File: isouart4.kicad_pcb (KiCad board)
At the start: 2 copper layers, 89 x 99 mm, 40 parts, among them J1 USB_B, J2 Conn_01x04, J3 Conn_01x04, J4 Conn_01x04, J5 Conn_01x04, U1 FT4232H, U10 74HC123, U11 74HC123, U12 74HC123, U13 74HC123, U2 93LCxxB, U3 AMS1117-3.3, U5 74HC595D, U6 π122U31, U7 π122U31, U8 π122U31, U9 π122U31, Y1 12.000 MHz

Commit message: Flush
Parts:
- added C10: 3.3uF, Capacitor_SMD:C_0805_2012Metric_Pad1.18x1.45mm_HandSolder, F.Cu at (166.9, 76.6)
- added C11: 3.3uF, Capacitor_SMD:C_0805_2012Metric_Pad1.18x1.45mm_HandSolder, F.Cu at (156.2, 73.5)
- added C12: 3.3uF, Capacitor_SMD:C_0805_2012Metric_Pad1.18x1.45mm_HandSolder, F.Cu at (166.1, 88.4)
- added C13: 1uF, Capacitor_SMD:C_0805_2012Metric_Pad1.18x1.45mm_HandSolder, F.Cu at (209.7, 64.0)
- added C14: 1uF, Capacitor_SMD:C_0805_2012Metric_Pad1.18x1.45mm_HandSolder, F.Cu at (213.9, 82.2)
- added C15: 1uF, Capacitor_SMD:C_0805_2012Metric_Pad1.18x1.45mm_HandSolder, F.Cu at (208.5, 90.9)
- added C16: 1uF, Capacitor_SMD:C_0805_2012Metric_Pad1.18x1.45mm_HandSolder, F.Cu at (210.4, 108.7)
- added C17: 1uF, Capacitor_SMD:C_0805_2012Metric_Pad1.18x1.45mm_HandSolder, F.Cu at (204.8, 62.5)
- added C18: 1uF, Capacitor_SMD:C_0805_2012Metric_Pad1.18x1.45mm_HandSolder, F.Cu at (213.9, 85.2)
- added C19: 1uF, Capacitor_SMD:C_0805_2012Metric_Pad1.18x1.45mm_HandSolder, F.Cu at (208.5, 93.9)
- added C20: 1uF, Capacitor_SMD:C_0805_2012Metric_Pad1.18x1.45mm_HandSolder, F.Cu at (210.4, 111.7)
- added C21: 1uF, Capacitor_SMD:C_0805_2012Metric_Pad1.18x1.45mm_HandSolder, B.Cu at (207.0, 68.8)
- added C22: 1uF, Capacitor_SMD:C_0805_2012Metric_Pad1.18x1.45mm_HandSolder, F.Cu at (205.1, 79.9)
- added C23: 1uF, Capacitor_SMD:C_0805_2012Metric_Pad1.18x1.45mm_HandSolder, F.Cu at (208.5, 96.9)
- added C24: 1uF, Capacitor_SMD:C_0805_2012Metric_Pad1.18x1.45mm_HandSolder, F.Cu at (210.4, 114.7)
- added C7: 3.3uF, Capacitor_SMD:C_0805_2012Metric_Pad1.18x1.45mm_HandSolder, F.Cu at (150.9, 79.8)
- added C8: 3.3uF, Capacitor_SMD:C_0805_2012Metric_Pad1.18x1.45mm_HandSolder, F.Cu at (160.3, 75.2)
- added C9: 3.3uF, Capacitor_SMD:C_0805_2012Metric_Pad1.18x1.45mm_HandSolder, F.Cu at (167.0, 84.7)
- added R10: 1k, Resistor_SMD:R_0805_2012Metric_Pad1.20x1.40mm_HandSolder, F.Cu at (205.7, 111.6)
- added R11: 220k, Resistor_SMD:R_0805_2012Metric_Pad1.20x1.40mm_HandSolder, F.Cu at (209.6, 59.8)
- added R12: 220k, Resistor_SMD:R_0805_2012Metric_Pad1.20x1.40mm_HandSolder, F.Cu at (200.3, 79.7)
- added R13: 220k, Resistor_SMD:R_0805_2012Metric_Pad1.20x1.40mm_HandSolder, F.Cu at (203.7, 96.8)
- added R14: 220k, Resistor_SMD:R_0805_2012Metric_Pad1.20x1.40mm_HandSolder, F.Cu at (205.7, 114.6)
- added R15: 220k, Resistor_SMD:R_0805_2012Metric_Pad1.20x1.40mm_HandSolder, F.Cu at (204.7, 58.1)
- added R16: 220k, Resistor_SMD:R_0805_2012Metric_Pad1.20x1.40mm_HandSolder, F.Cu at (200.3, 82.7)
- added R17: 220k, Resistor_SMD:R_0805_2012Metric_Pad1.20x1.40mm_HandSolder, F.Cu at (216.2, 103.5)
- added R18: 220k, Resistor_SMD:R_0805_2012Metric_Pad1.20x1.40mm_HandSolder, F.Cu at (205.7, 117.5)
- added R2: 1k, Resistor_SMD:R_0805_2012Metric_Pad1.20x1.40mm_HandSolder, F.Cu at (213.4, 51.8)
- added R4: 1k, Resistor_SMD:R_0805_2012Metric_Pad1.20x1.40mm_HandSolder, F.Cu at (209.1, 82.2)
- added R5: 1k, Resistor_SMD:R_0805_2012Metric_Pad1.20x1.40mm_HandSolder, F.Cu at (203.7, 90.9)
- added R6: 1k, Resistor_SMD:R_0805_2012Metric_Pad1.20x1.40mm_HandSolder, F.Cu at (205.7, 108.7)
- added R7: 1k, Resistor_SMD:R_0805_2012Metric_Pad1.20x1.40mm_HandSolder, F.Cu at (199.7, 51.8)
- added R8: 1k, Resistor_SMD:R_0805_2012Metric_Pad1.20x1.40mm_HandSolder, F.Cu at (209.1, 85.2)
- added R9: 1k, Resistor_SMD:R_0805_2012Metric_Pad1.20x1.40mm_HandSolder, F.Cu at (203.7, 93.8)
- C1, C2, C3, C4, C5, C6, L1, L2, R1, R3: moved to F.Cu
- U10, U11, U12, U13: moved to B.Cu
- moved D5 70.3 mm to (204.5, 50.8), turned to 0 degrees
- moved U13 60.3 mm to (207.9, 111.6), turned to 90 degrees
- moved D8 58.4 mm to (206.5, 121.7), turned to -90 degrees
- moved U10 51.6 mm to (207.1, 61.6)
- moved D6 31.8 mm to (204.4, 73.4), turned to 0 degrees
- moved U12 22.1 mm to (206.8, 94.1), turned to 90 degrees
- moved C6 17.2 mm to (150.9, 85.3), turned to 0 degrees
- moved J5 17.0 mm to (220.9, 124.4), turned to 90 degrees
- moved D7 15.7 mm to (206.9, 99.8), turned to -90 degrees
- moved J4 13.4 mm to (220.7, 103.7), turned to 90 degrees
- moved U11 9.65 mm to (207.1, 83.0), turned to -90 degrees
- moved C2 9.21 mm to (175.9, 89.9), turned to 180 degrees
- moved L2 8.83 mm to (172.4, 95.8)
- moved C3 7.21 mm to (156.3, 88.9), turned to 0 degrees
- moved C1 6.83 mm to (175.9, 85.0), turned to 180 degrees
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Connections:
- D5 pad 1: unconnected-(D5-K1-Pad1) -> Net-(D5-K1)
- D5 pad 2: unconnected-(D5-A-Pad2) -> /indicators-ch1/V+MON
- D5 pad 3: unconnected-(D5-K2-Pad3) -> Net-(D5-K2)
- D6 pad 1: unconnected-(D6-K1-Pad1) -> Net-(D6-K1)
- D6 pad 2: unconnected-(D6-A-Pad2) -> /indicators-ch2/V+MON
- D6 pad 3: unconnected-(D6-K2-Pad3) -> Net-(D6-K2)
- D7 pad 1: unconnected-(D7-K1-Pad1) -> Net-(D7-K1)
- D7 pad 2: unconnected-(D7-A-Pad2) -> /indicators-ch3/V+MON
- D7 pad 3: unconnected-(D7-K2-Pad3) -> Net-(D7-K2)
- D8 pad 1: unconnected-(D8-K1-Pad1) -> Net-(D8-K1)
- D8 pad 2: unconnected-(D8-A-Pad2) -> /indicators-ch4/V+MON
- D8 pad 3: unconnected-(D8-K2-Pad3) -> Net-(D8-K2)
- J2 pad 2: Net-(J2-Pin_2) -> /indicators-ch1/TXMON
- J2 pad 3: Net-(J2-Pin_3) -> /indicators-ch1/RXMON
- J2 pad 4: Net-(J2-Pin_4) -> /indicators-ch1/V+MON
- J3 pad 1: Net-(J3-Pin_1) -> /indicators-ch2/GNDMON
- J3 pad 2: Net-(J3-Pin_2) -> /indicators-ch2/TXMON
- J3 pad 3: Net-(J3-Pin_3) -> /indicators-ch2/RXMON
- J3 pad 4: Net-(J3-Pin_4) -> /indicators-ch2/V+MON
- J4 pad 1: Net-(J4-Pin_1) -> /indicators-ch3/GNDMON
- J4 pad 2: Net-(J4-Pin_2) -> /indicators-ch3/TXMON
- J4 pad 3: Net-(J4-Pin_3) -> /indicators-ch3/RXMON
- J4 pad 4: Net-(J4-Pin_4) -> /indicators-ch3/V+MON
- J5 pad 1: Net-(J5-Pin_1) -> /indicators-ch4/GNDMON
- J5 pad 2: Net-(J5-Pin_2) -> /indicators-ch4/TXMON
- J5 pad 3: Net-(J5-Pin_3) -> /indicators-ch4/RXMON
- J5 pad 4: Net-(J5-Pin_4) -> /indicators-ch4/V+MON
- U10 pad 1: unconnected-(U10A-A-Pad1) -> /indicators-ch1/TXMON
- U10 pad 10: unconnected-(U10B-B-Pad10) -> /indicators-ch1/V+MON
- U10 pad 11: unconnected-(U10B-Clr-Pad11) -> /indicators-ch1/V+MON
- U10 pad 12: unconnected-(U10B-~{Q}-Pad12) -> Net-(U10B-~{Q})
- U10 pad 14: unconnected-(U10A-Cext-Pad14) -> Net-(U10A-Cext)
- U10 pad 15: unconnected-(U10A-RCext-Pad15) -> Net-(U10A-RCext)
- U10 pad 16: unconnected-(U10C-VCC-Pad16) -> /indicators-ch1/V+MON
- U10 pad 2: unconnected-(U10A-B-Pad2) -> /indicators-ch1/V+MON
- U10 pad 3: unconnected-(U10A-Clr-Pad3) -> /indicators-ch1/V+MON
- U10 pad 4: unconnected-(U10A-~{Q}-Pad4) -> Net-(U10A-~{Q})
- U10 pad 6: unconnected-(U10B-Cext-Pad6) -> Net-(U10B-Cext)
- U10 pad 7: unconnected-(U10B-RCext-Pad7) -> Net-(U10B-RCext)
- U10 pad 8: unconnected-(U10C-GND-Pad8) -> /indicators-ch1/GNDMON
- U10 pad 9: unconnected-(U10B-A-Pad9) -> /indicators-ch1/RXMON
- U11 pad 1: unconnected-(U11A-A-Pad1) -> /indicators-ch2/TXMON
- U11 pad 10: unconnected-(U11B-B-Pad10) -> /indicators-ch2/V+MON
- U11 pad 11: unconnected-(U11B-Clr-Pad11) -> /indicators-ch2/V+MON
- U11 pad 12: unconnected-(U11B-~{Q}-Pad12) -> Net-(U11B-~{Q})
- U11 pad 14: unconnected-(U11A-Cext-Pad14) -> Net-(U11A-Cext)
- U11 pad 15: unconnected-(U11A-RCext-Pad15) -> Net-(U11A-RCext)
- U11 pad 16: unconnected-(U11C-VCC-Pad16) -> /indicators-ch2/V+MON
- U11 pad 2: unconnected-(U11A-B-Pad2) -> /indicators-ch2/V+MON
- U11 pad 3: unconnected-(U11A-Clr-Pad3) -> /indicators-ch2/V+MON
- U11 pad 4: unconnected-(U11A-~{Q}-Pad4) -> Net-(U11A-~{Q})
- U11 pad 6: unconnected-(U11B-Cext-Pad6) -> Net-(U11B-Cext)
- U11 pad 7: unconnected-(U11B-RCext-Pad7) -> Net-(U11B-RCext)
- U11 pad 8: unconnected-(U11C-GND-Pad8) -> /indicators-ch2/GNDMON
- U11 pad 9: unconnected-(U11B-A-Pad9) -> /indicators-ch2/RXMON
- U12 pad 1: unconnected-(U12A-A-Pad1) -> /indicators-ch3/TXMON
- U12 pad 10: unconnected-(U12B-B-Pad10) -> /indicators-ch3/V+MON
- U12 pad 11: unconnected-(U12B-Clr-Pad11) -> /indicators-ch3/V+MON
- U12 pad 12: unconnected-(U12B-~{Q}-Pad12) -> Net-(U12B-~{Q})
- U12 pad 14: unconnected-(U12A-Cext-Pad14) -> Net-(U12A-Cext)
- U12 pad 15: unconnected-(U12A-RCext-Pad15) -> Net-(U12A-RCext)
- U12 pad 16: unconnected-(U12C-VCC-Pad16) -> /indicators-ch3/V+MON
- U12 pad 2: unconnected-(U12A-B-Pad2) -> /indicators-ch3/V+MON
- U12 pad 3: unconnected-(U12A-Clr-Pad3) -> /indicators-ch3/V+MON
- U12 pad 4: unconnected-(U12A-~{Q}-Pad4) -> Net-(U12A-~{Q})
- U12 pad 6: unconnected-(U12B-Cext-Pad6) -> Net-(U12B-Cext)
- U12 pad 7: unconnected-(U12B-RCext-Pad7) -> Net-(U12B-RCext)
- U12 pad 8: unconnected-(U12C-GND-Pad8) -> /indicators-ch3/GNDMON
- U12 pad 9: unconnected-(U12B-A-Pad9) -> /indicators-ch3/RXMON
- U13 pad 1: unconnected-(U13A-A-Pad1) -> /indicators-ch4/TXMON
- U13 pad 10: unconnected-(U13B-B-Pad10) -> /indicators-ch4/V+MON
- U13 pad 11: unconnected-(U13B-Clr-Pad11) -> /indicators-ch4/V+MON
- U13 pad 12: unconnected-(U13B-~{Q}-Pad12) -> Net-(U13B-~{Q})
- U13 pad 14: unconnected-(U13A-Cext-Pad14) -> Net-(U13A-Cext)
- U13 pad 15: unconnected-(U13A-RCext-Pad15) -> Net-(U13A-RCext)
- U13 pad 16: unconnected-(U13C-VCC-Pad16) -> /indicators-ch4/V+MON
- U13 pad 2: unconnected-(U13A-B-Pad2) -> /indicators-ch4/V+MON
- U13 pad 3: unconnected-(U13A-Clr-Pad3) -> /indicators-ch4/V+MON
- U13 pad 4: unconnected-(U13A-~{Q}-Pad4) -> Net-(U13A-~{Q})
- U13 pad 6: unconnected-(U13B-Cext-Pad6) -> Net-(U13B-Cext)
- U13 pad 7: unconnected-(U13B-RCext-Pad7) -> Net-(U13B-RCext)
- U13 pad 8: unconnected-(U13C-GND-Pad8) -> /indicators-ch4/GNDMON
- U13 pad 9: unconnected-(U13B-A-Pad9) -> /indicators-ch4/RXMON
- U6 pad 6: Net-(J2-Pin_2) -> /indicators-ch1/TXMON
- U6 pad 7: Net-(J2-Pin_3) -> /indicators-ch1/RXMON
- U6 pad 8: Net-(J2-Pin_4) -> /indicators-ch1/V+MON
- U7 pad 5: Net-(J3-Pin_1) -> /indicators-ch2/GNDMON
- U7 pad 6: Net-(J3-Pin_2) -> /indicators-ch2/TXMON
- U7 pad 7: Net-(J3-Pin_3) -> /indicators-ch2/RXMON
- U7 pad 8: Net-(J3-Pin_4) -> /indicators-ch2/V+MON
- U8 pad 5: Net-(J4-Pin_1) -> /indicators-ch3/GNDMON
- U8 pad 6: Net-(J4-Pin_2) -> /indicators-ch3/TXMON
- U8 pad 7: Net-(J4-Pin_3) -> /indicators-ch3/RXMON
- U8 pad 8: Net-(J4-Pin_4) -> /indicators-ch3/V+MON
- U9 pad 5: Net-(J5-Pin_1) -> /indicators-ch4/GNDMON
- U9 pad 6: Net-(J5-Pin_2) -> /indicators-ch4/TXMON
- U9 pad 7: Net-(J5-Pin_3) -> /indicators-ch4/RXMON
- U9 pad 8: Net-(J5-Pin_4) -> /indicators-ch4/V+MON
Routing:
- net /indicators-ch1/V+MON: track 0.00 -> 77.1 mm, vias 0 -> 4
- net /indicators-ch1/TXMON: track 0.00 -> 31.6 mm, vias 0 -> 2
- net /indicators-ch1/RXMON: track 0.00 -> 29.8 mm, vias 0 -> 2
- net Net-(J2-Pin_1): track 0.00 -> 29.1 mm, vias 0 -> 2
- net /USB2-UART4/TX1: track 107.5 -> 91.4 mm
- net Net-(U10B-~{Q}): track 0.00 -> 12.1 mm, vias 0 -> 1
- net Net-(U10A-~{Q}): track 0.00 -> 11.2 mm, vias 0 -> 1
- net Net-(U10B-RCext): track 0.00 -> 9.83 mm, vias 0 -> 1
- net /indicators-ch1/GNDMON: track 0.00 -> 9.62 mm
- net /USB2-UART4/VIN 3.3V: track 278.8 -> 269.5 mm, vias 10 -> 11
- net Net-(U1-VREGOUT): track 54.2 -> 46.7 mm, vias 5 -> 4
- net Net-(U10A-RCext): track 0.00 -> 7.01 mm, vias 0 -> 1
- net Net-(U10A-Cext): track 0.00 -> 6.71 mm, vias 0 -> 1
- net /USB2-UART4/VPLL +3.3V: track 17.8 -> 12.1 mm, vias 0 -> 1
- net GND: track 81.9 -> 76.6 mm, vias 18 -> 13
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
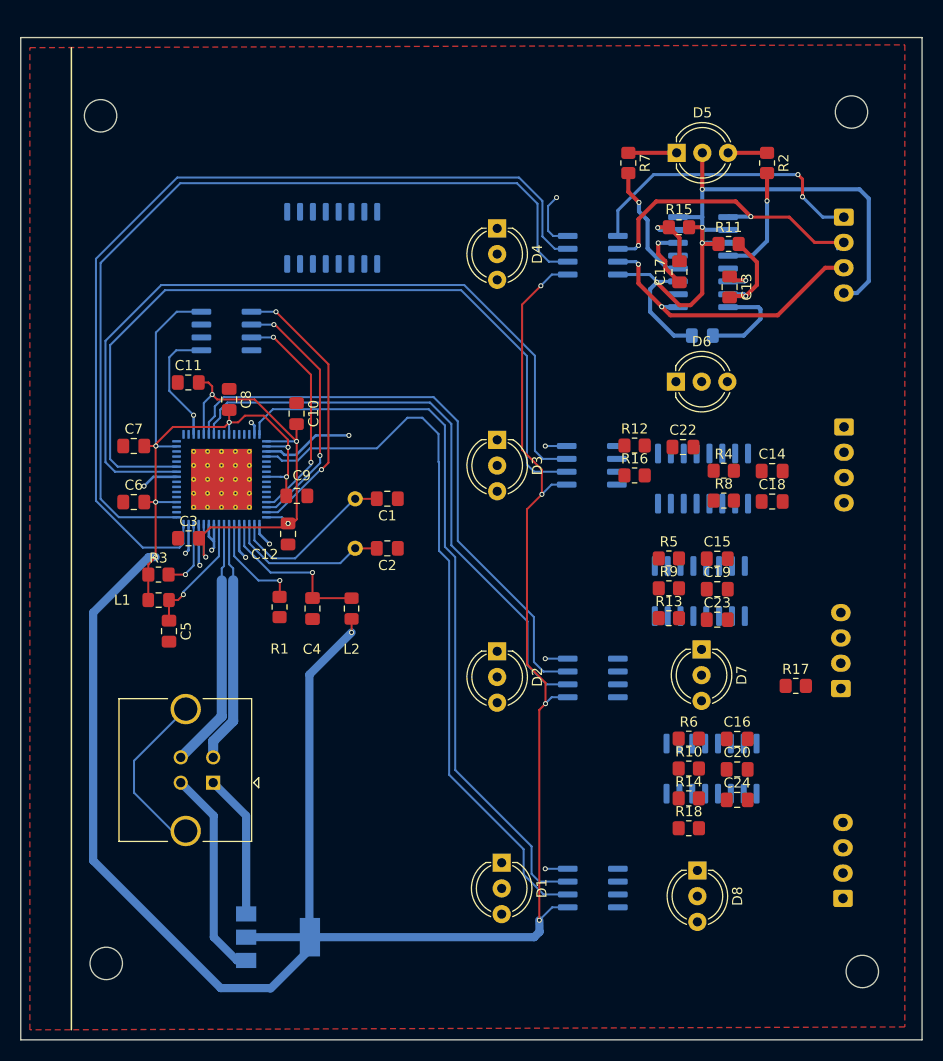
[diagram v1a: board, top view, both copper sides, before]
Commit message: switch to CH344Q
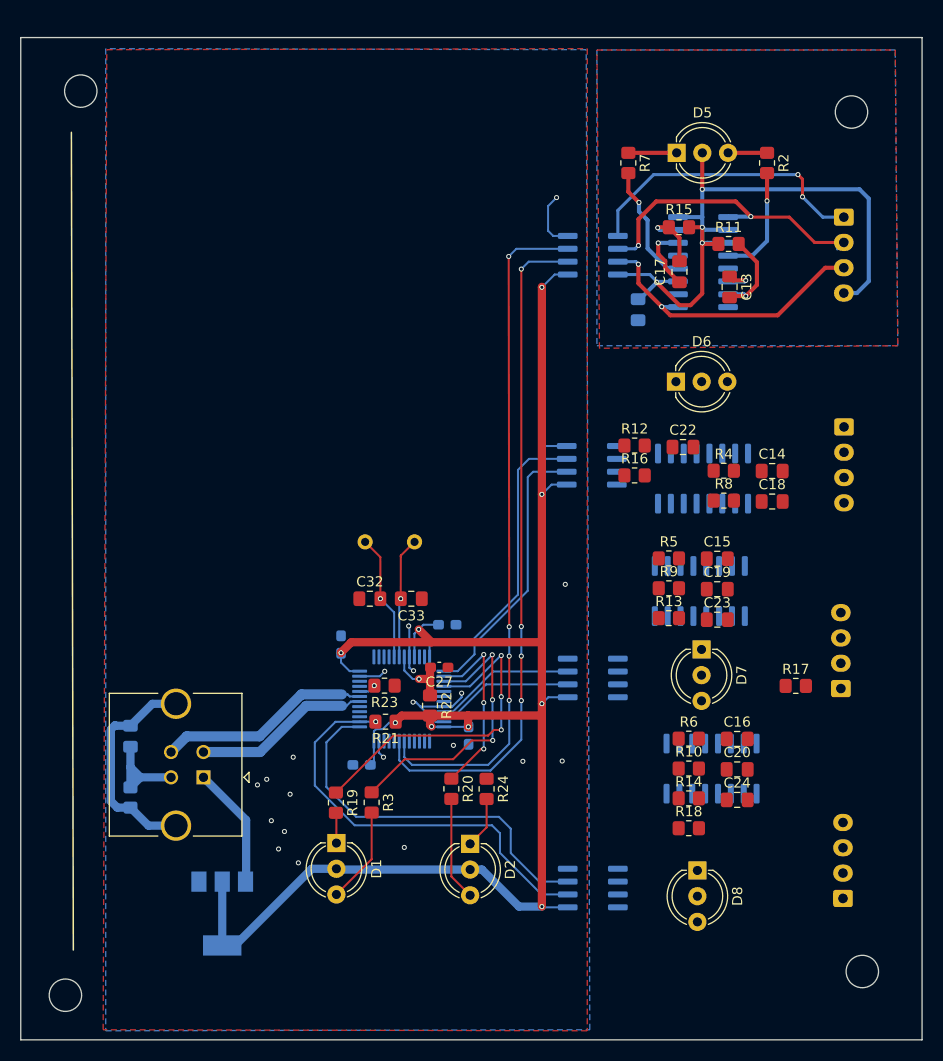
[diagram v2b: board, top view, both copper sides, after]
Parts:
- removed C10, C11, C12, C3, C4, C5, C6, C7, C8, C9: 3.3uF, Capacitor_SMD:C_0805_2012Metric_Pad1.18x1.45mm_HandSolder
- removed C2: 30pF, Capacitor_SMD:C_0805_2012Metric_Pad1.18x1.45mm_HandSolder
- removed D3, D4: LED_Dual_KAK, LED_THT:LED_D5.0mm-3
- removed L1, L2: L_Iron, Inductor_SMD:L_0805_2012Metric_Pad1.15x1.40mm_HandSolder
- removed U2: 93LCxxB, Package_SO:SOIC-8_3.9x4.9mm_P1.27mm
- removed U5: 74HC595D, Package_SO:SO-16_3.9x9.9mm_P1.27mm
- removed Y1: 12.000 MHz, Crystal:Crystal_HC49-U_Vertical
- added C27: 100n, Capacitor_SMD:C_0603_1608Metric_Pad1.08x0.95mm_HandSolder, F.Cu at (181.0, 101.6)
- added C28: 100n, Capacitor_SMD:C_0603_1608Metric_Pad1.08x0.95mm_HandSolder, B.Cu at (181.8, 97.4)
- added C29: 100n, Capacitor_SMD:C_0603_1608Metric_Pad1.08x0.95mm_HandSolder, B.Cu at (183.9, 108.4)
- added C30: 100n, Capacitor_SMD:C_0603_1608Metric_Pad1.08x0.95mm_HandSolder, B.Cu at (173.4, 111.3)
- added C31: 100n, Capacitor_SMD:C_0603_1608Metric_Pad1.08x0.95mm_HandSolder, B.Cu at (171.3, 99.4)
- added C32: 22p, Capacitor_SMD:C_0805_2012Metric_Pad1.18x1.45mm_HandSolder, F.Cu at (174.2, 94.8)
- added C33: 22p, Capacitor_SMD:C_0805_2012Metric_Pad1.18x1.45mm_HandSolder, F.Cu at (178.3, 94.8)
- added R19: 1k, Resistor_SMD:R_0805_2012Metric_Pad1.20x1.40mm_HandSolder, F.Cu at (170.8, 115.0)
- added R20: 1k, Resistor_SMD:R_0805_2012Metric_Pad1.20x1.40mm_HandSolder, F.Cu at (182.2, 113.6)
- added R21: 4k7, Resistor_SMD:R_0805_2012Metric_Pad1.20x1.40mm_HandSolder, F.Cu at (175.7, 107.0)
- added R22: 4k7, Resistor_SMD:R_0805_2012Metric_Pad1.20x1.40mm_HandSolder, F.Cu at (180.1, 105.4)
- added R23: 4k7, Resistor_SMD:R_0805_2012Metric_Pad1.20x1.40mm_HandSolder, F.Cu at (175.6, 103.4)
- added R24: 1k, Resistor_SMD:R_0805_2012Metric_Pad1.20x1.40mm_HandSolder, F.Cu at (185.7, 113.6)
- added Y2: 8MHz, Crystal:Crystal_HC49-U_Vertical, B.Cu at (173.7, 89.2)
- C1: value 30pF -> 4n7; moved to B.Cu
- R1: value 12k 1% -> 1M; moved to B.Cu
- U1: value FT4232H -> CH344Q; footprint Package_DFN_QFN:QFN-64-1EP_9x9mm_P0.5mm_EP6x6mm_ThermalVias -> Package_QFP:LQFP-48_7x7mm_P0.5mm
- moved C1 34.6 mm to (150.5, 108.4), turned to 90 degrees
- moved R3 30.8 mm to (174.3, 115.0), turned to -90 degrees
- moved U1 28.1 mm to (177.3, 104.7), turned to -90 degrees
- moved R1 23.9 mm to (150.5, 114.5)
- moved D2 19.2 mm to (184.1, 119.0)
- moved D1 16.4 mm to (170.9, 119.0)
- moved C21 6.85 mm to (200.7, 66.3), turned to 90 degrees
- moved U3 5.99 mm to (159.6, 125.9), turned to -90 degrees
- moved H1 5.11 mm to (144.1, 134.0)
- moved H4 3.13 mm to (145.6, 44.7)
- moved J1 1.09 mm to (157.7, 112.5)
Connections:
- C1 pad 2: Net-(U1-OSCI) -> Net-(J1-Shield)
- D1 pad 1: unconnected-(D1-K1-Pad1) -> Net-(D1-K1)
- D1 pad 2: unconnected-(D1-A-Pad2) -> /USB-UART4-CH344Q/VIN 3.3V
- D1 pad 3: unconnected-(D1-K2-Pad3) -> Net-(D1-K2)
- D2 pad 1: unconnected-(D2-K1-Pad1) -> Net-(D2-K1)
- D2 pad 2: unconnected-(D2-A-Pad2) -> /USB-UART4-CH344Q/VIN 3.3V
- D2 pad 3: unconnected-(D2-K2-Pad3) -> Net-(D2-K2)
- J1 pad 2: /USB2-UART4/D- -> /USB-UART4-CH344Q/USB_N
- J1 pad 3: /USB2-UART4/D+ -> /USB-UART4-CH344Q/USB_P
- J1 pad 5: unconnected-(J1-Shield-Pad5) -> Net-(J1-Shield)
- J2 pad 1: Net-(J2-Pin_1) -> /indicators-ch1/GNDMON
- R1 pad 1: Net-(U1-REF) -> GND
- R1 pad 2: GND -> Net-(J1-Shield)
- R3 pad 1: /USB2-UART4/VIN 3.3V -> /USB-UART4-CH344Q/TX_S
- R3 pad 2: Net-(U1-~{RESET}) -> Net-(D1-K2)
- U1 pad 1: GND -> unconnected-(U1A-NC-Pad1)
- U1 pad 10: GND -> unconnected-(U1C-GPIO2|CTS1-Pad10)
- U1 pad 11: GND -> unconnected-(U1C-GPIO3|RTS1-Pad11)
- U1 pad 12: Net-(U1-VREGOUT) -> /USB-UART4-CH344Q/TXD1_INT
- U1 pad 13: GND -> /USB-UART4-CH344Q/RXD1_INT
- U1 pad 14: Net-(U1-~{RESET}) -> /USB-UART4-CH344Q/ACT
- U1 pad 15: GND -> /USB-UART4-CH344Q/TX_S
- U1 pad 16: /USB2-UART4/TX1 -> /USB-UART4-CH344Q/RX_S
- U1 pad 17: /USB2-UART4/RX1 -> unconnected-(U1C-DSR1-Pad17)
- U1 pad 2: Net-(U1-OSCI) -> unconnected-(U1D-DSR2-Pad2)
- U1 pad 20: /USB2-UART4/VIN 3.3V -> GND
- U1 pad 21: unconnected-(U1-ADBUS4-Pad21) -> /USB-UART4-CH344Q/TXD2_INT
- U1 pad 22: unconnected-(U1-ADBUS5-Pad22) -> /USB-UART4-CH344Q/RXD2_INT
- U1 pad 23: unconnected-(U1-ADBUS6-Pad23) -> GND
- U1 pad 24: unconnected-(U1-ADBUS7-Pad24) -> /USB-UART4-CH344Q/VIN 3.3V
- U1 pad 25: GND -> unconnected-(U1C-RI1-Pad25)
- U1 pad 26: /USB2-UART4/TX2 -> unconnected-(U1D-GPIO4|CTS2-Pad26)
- U1 pad 27: /USB2-UART4/RX2 -> unconnected-(U1D-GPIO5|RTS2-Pad27)
- U1 pad 3: Net-(U1-OSCO) -> unconnected-(U1D-RI2-Pad3)
- U1 pad 30: unconnected-(U1-BDBUS4-Pad30) -> /USB-UART4-CH344Q/TXD0_INT
- U1 pad 31: /USB2-UART4/VIN 3.3V -> /USB-UART4-CH344Q/RXD0_INT
- U1 pad 36: unconnected-(U1-~{SUSPEND}-Pad36) -> /USB-UART4-CH344Q/VIN 3.3V
- U1 pad 37: Net-(U1-VREGOUT) -> /USB-UART4-CH344Q/TXD3_INT
- U1 pad 38: /USB2-UART4/TX3 -> /USB-UART4-CH344Q/RXD3_INT
- U1 pad 39: /USB2-UART4/RX3 -> unconnected-(U1B-GPIO8|TNOW0|DTR0-Pad39)
- U1 pad 4: /USB2-UART4/VPHY +3.3V -> unconnected-(U1D-DCD2-Pad4)
- U1 pad 42: /USB2-UART4/VIN 3.3V -> /USB-UART4-CH344Q/USB_N
- U1 pad 43: unconnected-(U1-CDBUS4-Pad43) -> /USB-UART4-CH344Q/USB_P
- U1 pad 44: unconnected-(U1-CDBUS5-Pad44) -> /USB-UART4-CH344Q/TEST
- U1 pad 48: /USB2-UART4/TX4 -> /USB-UART4-CH344Q/VIN 3.3V
- U1 pad 5: GND -> /USB-UART4-CH344Q/XI
- U1 pad 6: Net-(U1-REF) -> /USB-UART4-CH344Q/XO
- U1 pad 7: /USB2-UART4/D- -> /USB-UART4-CH344Q/RESET
- U1 pad 8: /USB2-UART4/D+ -> GND
- U1 pad 9: /USB2-UART4/VPLL +3.3V -> /USB-UART4-CH344Q/VIN 3.3V
- U3 pad 2: /USB2-UART4/VIN 3.3V -> /USB-UART4-CH344Q/VIN 3.3V
- U6 pad 1: /USB2-UART4/VIN 3.3V -> /USB-UART4-CH344Q/VIN 3.3V
- U6 pad 2: /USB2-UART4/RX1 -> /USB-UART4-CH344Q/RXD0_INT
- U6 pad 3: /USB2-UART4/TX1 -> /USB-UART4-CH344Q/TXD0_INT
- U6 pad 5: Net-(J2-Pin_1) -> /indicators-ch1/GNDMON
- U7 pad 1: /USB2-UART4/VIN 3.3V -> /USB-UART4-CH344Q/VIN 3.3V
- U7 pad 2: /USB2-UART4/RX2 -> /USB-UART4-CH344Q/RXD1_INT
- U7 pad 3: /USB2-UART4/TX2 -> /USB-UART4-CH344Q/TXD1_INT
- U8 pad 1: /USB2-UART4/VIN 3.3V -> /USB-UART4-CH344Q/VIN 3.3V
- U8 pad 2: /USB2-UART4/RX3 -> /USB-UART4-CH344Q/RXD2_INT
- U8 pad 3: /USB2-UART4/TX3 -> /USB-UART4-CH344Q/TXD2_INT
- U9 pad 1: /USB2-UART4/VIN 3.3V -> /USB-UART4-CH344Q/VIN 3.3V
- U9 pad 2: /USB2-UART4/RX4 -> /USB-UART4-CH344Q/RXD3_INT
- U9 pad 3: /USB2-UART4/TX4 -> /USB-UART4-CH344Q/TXD3_INT
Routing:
- net /USB2-UART4/VIN 3.3V: track 269.5 -> 0.00 mm, vias 11 -> 0
- net /USB-UART4-CH344Q/VIN 3.3V: track 0.00 -> 172.1 mm, vias 0 -> 9
- net /USB2-UART4/TX1: track 91.4 -> 0.00 mm
- net /USB2-UART4/RX1: track 86.9 -> 0.00 mm
- net /USB2-UART4/TX2: track 79.9 -> 0.00 mm
- net /USB2-UART4/RX2: track 79.2 -> 0.00 mm
- net /USB2-UART4/TX4: track 72.4 -> 0.00 mm
- net /USB2-UART4/RX4: track 71.8 -> 0.00 mm
- net /USB-UART4-CH344Q/TXD0_INT: track 0.00 -> 67.5 mm, vias 0 -> 4
- net /USB-UART4-CH344Q/RXD0_INT: track 0.00 -> 67.1 mm, vias 0 -> 4
- net /USB2-UART4/TX3: track 59.0 -> 0.00 mm
- net /USB2-UART4/RX3: track 58.4 -> 0.00 mm
- net Net-(U1-VREGOUT): track 46.7 -> 0.00 mm, vias 4 -> 0
- net /USB-UART4-CH344Q/RXD3_INT: track 0.00 -> 41.7 mm, vias 0 -> 1
- net GND: track 76.6 -> 35.9 mm, vias 13 -> 20
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- added copper zone on B.Cu, net /indicators-ch1/GNDMON
- added copper zone on F.Cu, net /indicators-ch1/GNDMON
- added copper zone on B.Cu, net GND

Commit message: More feng shui
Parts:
- removed C32, C33: 22p, Capacitor_SMD:C_0805_2012Metric_Pad1.18x1.45mm_HandSolder
- removed U7, U8, U9: π122U31, Package_SO:SOIC-8_3.9x4.9mm_P1.27mm
- removed Y2: 8MHz, Crystal:Crystal_HC49-U_Vertical
- added C2: 10uF, Capacitor_SMD:C_0805_2012Metric_Pad1.18x1.45mm_HandSolder, B.Cu at (167.0, 66.6)
- added C3: 100n, Capacitor_SMD:C_0603_1608Metric_Pad1.08x0.95mm_HandSolder, F.Cu at (192.0, 84.5)
- added C4: 100n, Capacitor_SMD:C_0805_2012Metric_Pad1.18x1.45mm_HandSolder, B.Cu at (170.5, 97.0)
- added C5: 100n, Capacitor_SMD:C_0805_2012Metric_Pad1.18x1.45mm_HandSolder, B.Cu at (171.4, 87.9)
- added C6: 12p, Capacitor_SMD:C_0805_2012Metric_Pad1.18x1.45mm_HandSolder, B.Cu at (170.6, 109.4)
- added C7: 10uF, Capacitor_SMD:C_0805_2012Metric_Pad1.18x1.45mm_HandSolder, B.Cu at (170.4, 66.6)
- added L1: L_Ferrite_Small, Inductor_SMD:L_TDK_NLV25_2.5x2.0mm, B.Cu at (152.7, 107.1)
- added L2: L_Ferrite_Small, Inductor_SMD:L_TDK_NLV25_2.5x2.0mm, B.Cu at (163.8, 123.0)
- added L3: L_Ferrite_Small, Inductor_SMD:L_TDK_NLV25_2.5x2.0mm, B.Cu at (169.5, 93.0)
- added L4: L_Ferrite_Small, Inductor_SMD:L_TDK_NLV25_2.5x2.0mm, B.Cu at (177.7, 106.8)
- added U2: π122U31, Package_SO:SOIC-8_3.9x4.9mm_P1.27mm, B.Cu at (196.1, 81.6)
- added U4: π122U31, Package_SO:SOIC-8_3.9x4.9mm_P1.27mm, B.Cu at (196.2, 102.7)
- added U5: π122U31, Package_SO:SOIC-8_3.9x4.9mm_P1.27mm, B.Cu at (196.2, 123.4)
- added X1: ASV-xxxMHz, Oscillator:Oscillator_SMD_Abracon_ASV-4Pin_7.0x5.1mm, B.Cu at (171.5, 104.0)
- C27: footprint Capacitor_SMD:C_0603_1608Metric_Pad1.08x0.95mm_HandSolder -> Capacitor_SMD:C_0805_2012Metric_Pad1.18x1.45mm_HandSolder
- moved U3 66.9 mm to (169.3, 59.8), turned to 90 degrees
- moved D2 52.4 mm to (158.3, 73.4), turned to 0 degrees
- moved D1 46.9 mm to (182.8, 73.6), turned to 180 degrees
- moved R24 41.9 mm to (158.3, 81.9), turned to 90 degrees
- moved R20 37.8 mm to (161.5, 81.9), turned to 90 degrees
- moved R19 36.3 mm to (182.0, 80.5), turned to 90 degrees
- moved R3 34.6 mm to (177.7, 80.5), turned to 90 degrees
- moved R21 22.5 mm to (188.1, 125.8)
- moved C27 17.8 mm to (171.1, 116.5), turned to 90 degrees
- moved C28 15.1 mm to (175.9, 111.3)
- moved C29 15.0 mm to (175.9, 121.0), turned to 180 degrees
- moved R23 14.5 mm to (169.1, 116.4), turned to 90 degrees
- moved C30 13.9 mm to (167.2, 123.7), turned to 90 degrees
- moved U1 13.6 mm to (170.3, 116.3)
- moved C31 13.1 mm to (164.9, 110.8)
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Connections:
- net /USB-UART4-CH344Q/RXD0_INT renamed /USB-UART4-CH344Q/RX1
- net /USB-UART4-CH344Q/RXD3_INT renamed /USB-UART4-CH344Q/RX4
- net /USB-UART4-CH344Q/TXD0_INT renamed /USB-UART4-CH344Q/TX1
- net /USB-UART4-CH344Q/USB_N renamed /USB-UART4-CH344Q/D-
- net /USB-UART4-CH344Q/USB_P renamed /USB-UART4-CH344Q/D+
- net Net-(J1-Shield) renamed /USBSHLD
- C28 pad 2: /USB-UART4-CH344Q/VIN 3.3V -> Net-(C28-Pad2)
- C29 pad 2: /USB-UART4-CH344Q/VIN 3.3V -> Net-(C28-Pad2)
- C30 pad 2: /USB-UART4-CH344Q/VIN 3.3V -> Net-(C28-Pad2)
- C31 pad 2: /USB-UART4-CH344Q/VIN 3.3V -> Net-(C28-Pad2)
- J1 pad 4: GND -> /GNDUSBCONN
- R22 pad 2: /USB-UART4-CH344Q/VIN 3.3V -> Net-(C28-Pad2)
- U1 pad 12: /USB-UART4-CH344Q/TXD1_INT -> /USB-UART4-CH344Q/TX2
- U1 pad 13: /USB-UART4-CH344Q/RXD1_INT -> /USB-UART4-CH344Q/RX2
- U1 pad 21: /USB-UART4-CH344Q/TXD2_INT -> /USB-UART4-CH344Q/TX3
- U1 pad 22: /USB-UART4-CH344Q/RXD2_INT -> /USB-UART4-CH344Q/RX3
- U1 pad 24: /USB-UART4-CH344Q/VIN 3.3V -> Net-(C28-Pad2)
- U1 pad 36: /USB-UART4-CH344Q/VIN 3.3V -> Net-(C28-Pad2)
- U1 pad 37: /USB-UART4-CH344Q/TXD3_INT -> /USB-UART4-CH344Q/TX4
- U1 pad 48: /USB-UART4-CH344Q/VIN 3.3V -> Net-(C28-Pad2)
- U1 pad 9: /USB-UART4-CH344Q/VIN 3.3V -> Net-(C28-Pad2)
- U3 pad 3: Net-(J1-VBUS) -> Net-(U3-VI)
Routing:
- net Net-(U3-VI): track 0.00 -> 55.5 mm
- net /USB-UART4-CH344Q/TX2: track 0.00 -> 49.5 mm, vias 0 -> 2
- net /USB-UART4-CH344Q/RX2: track 0.00 -> 47.2 mm, vias 0 -> 2
- net /USB-UART4-CH344Q/ACT: track 18.6 -> 58.9 mm, vias 3 -> 1
- net Net-(C28-Pad2): track 0.00 -> 39.8 mm, vias 0 -> 1
- net /USB-UART4-CH344Q/TXD3_INT: track 37.5 -> 0.00 mm
- net /USB-UART4-CH344Q/TX4: track 0.00 -> 29.6 mm, vias 0 -> 2
- net /USB-UART4-CH344Q/TXD1_INT: track 29.6 -> 0.00 mm
- net /USB-UART4-CH344Q/TX3: track 0.00 -> 29.5 mm
- net /USB-UART4-CH344Q/RX3: track 0.00 -> 29.1 mm
- net /USB-UART4-CH344Q/RXD1_INT: track 27.5 -> 0.00 mm
- net /USB-UART4-CH344Q/TX_S: track 28.4 -> 47.7 mm, vias 3 -> 1
- net /USB-UART4-CH344Q/VIN 3.3V: track 172.1 -> 191.2 mm, vias 9 -> 25
- net /GNDUSBCONN: track 0.00 -> 18.8 mm
- net /USB-UART4-CH344Q/TXD2_INT: track 13.9 -> 0.00 mm
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- added copper zone on B.Cu, net /USB-UART4-CH344Q/VIN 3.3V
- added copper zone on F.Cu, net /USB-UART4-CH344Q/VIN 3.3V
- added copper zone on F.Cu, net /USBSHLD
